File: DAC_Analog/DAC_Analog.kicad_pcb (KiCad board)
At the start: 2 copper layers, 100 x 100 mm, 146 parts, among them J1 SPDIF_RX_1, J2 SPDIF_RX_2, J3 SPDIF_RX_3, J4 SPDIF_RX_4, J5 I2C_IN, J6 OutR, J7 OutL, J8 Conn_01x06, J9 Conn_01x04, T1 DA103C, T2 DA103C, T3 DA103C, T4 DA103C, U1 ISO154x, U10 OPA627xx, U11 TC595002ECB, U12 TPS79318, U13 SRC4392, U14 TPS79333, U15 TPS79333, U16 REG104_DCQ, U17 PCM1792A, U18 DS90LV012ATMF, U19 LMK61E2, U2 OPA627xx, U3 OPA627xx, U4 REG104_DCQ, U5 OPA627xx, U6 TC595002ECB, U7 OPA627xx, U8 OPA627xx, U9 REG104_DCQ

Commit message: update footprint
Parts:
- J1, J2, J3, J4, J6, J7: footprint Yame_library:HE10_14-2C-2.54-MR -> Pin_Headers:Pin_Header_Straight_1x02_Pitch2.54mm
- J5, J9: footprint Yame_library:HE10_14-4C-2.54-MR -> Pin_Headers:Pin_Header_Straight_1x04_Pitch2.54mm
- J8: footprint Yame_library:HE10_14-6C-2.54-MR -> Pin_Headers:Pin_Header_Straight_1x06_Pitch2.54mm
- moved J3 43.2 mm to (130.0, 103.0)
- moved J9 35.3 mm to (153.0, 44.0)
- moved J4 21.9 mm to (154.0, 98.0)
- moved J2 10.0 mm to (136.0, 91.0)
- moved J5 4.00 mm to (131.0, 52.0)
- moved J8 3.67 mm to (135.0, 55.0)

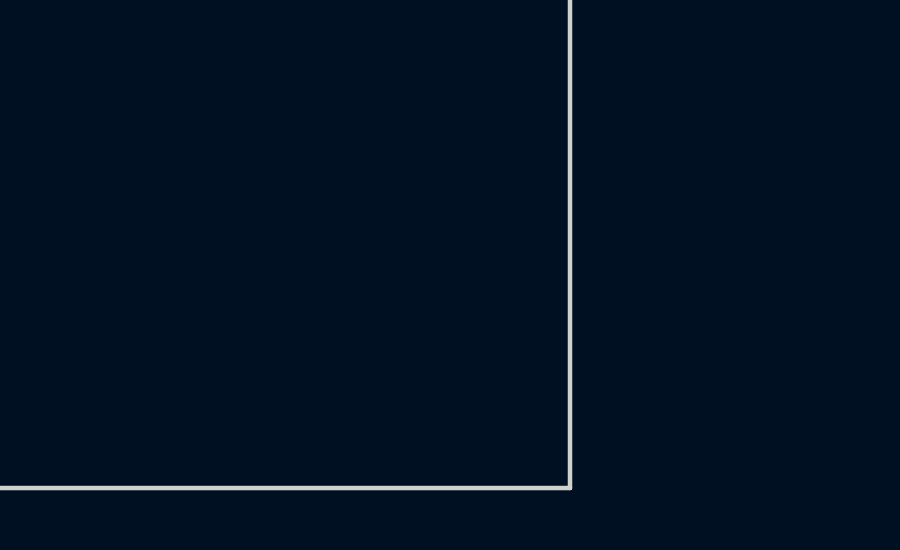
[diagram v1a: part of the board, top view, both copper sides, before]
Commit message: place all components on DAC_Analog
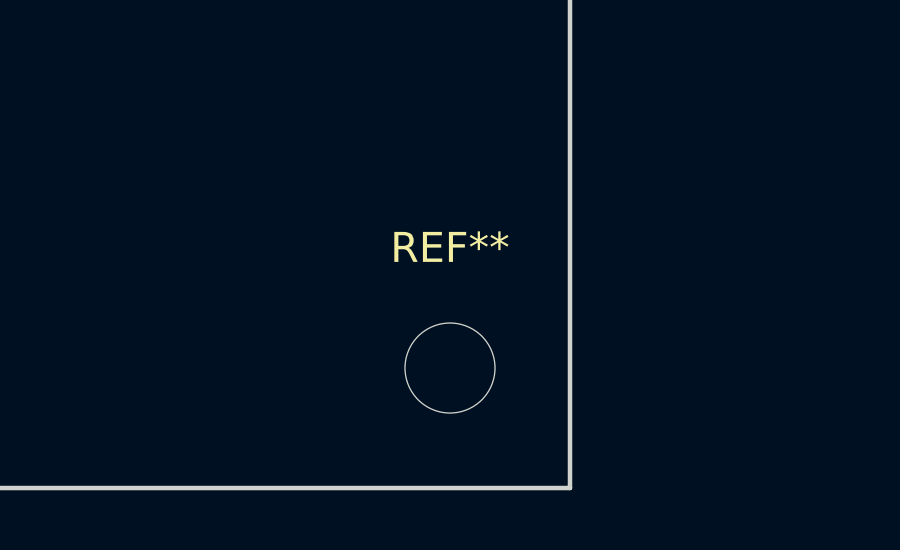
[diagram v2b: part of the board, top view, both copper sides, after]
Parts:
- added REF**: MountingHole_3mm, Mounting_Holes:MountingHole_3mm, F.Cu at (145.0, 145.0)
- J8: value Conn_01x06 -> Alim_DAC
- J9: value Conn_01x04 -> Alim_SRC
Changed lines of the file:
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@@
     (tracks 0)
     (zones 0)
-    (modules 146)
+    (modules 147)
     (nets 123)
   )
@@
       (effects (font (size 1 1) (thickness 0.15)))
     )
-    (fp_text value Conn_01x06 (at 0 15.03) (layer F.Fab)
+    (fp_text value Alim_DAC (at 0 15.03) (layer F.Fab)
       (effects (font (size 1 1) (thickness 0.15)))
     )
@@
       (effects (font (size 1 1) (thickness 0.15)))
     )
-    (fp_text value Conn_01x04 (at 0 9.95) (layer F.Fab)
+    (fp_text value Alim_SRC (at 0 9.95) (layer F.Fab)
       (effects (font (size 1 1) (thickness 0.15)))
     )
@@
     )
   )
+  (module Mounting_Holes:MountingHole_3mm (layer F.Cu)
+    (at 145 145)
+    (descr "Mounting Hole 3mm, no annular")
+    (tags "mounting hole 3mm no annular")
+    (attr virtual)
+    (fp_text reference REF** (at 0 -4) (layer F.SilkS)
+      (effects (font (size 1 1) (thickness 0.15)))
+    )
+    (fp_text value MountingHole_3mm (at 0 4) (layer F.Fab)
+      (effects (font (size 1 1) (thickness 0.15)))
+    )
+    (fp_text user %R (at 0.3 0) (layer F.Fab)
+      (effects (font (size 1 1) (thickness 0.15)))
+    )
+    (fp_circle (center 0 0) (end 3 0) (layer Cmts.User) (width 0.15))
+    (fp_circle (center 0 0) (end 3.25 0) (layer F.CrtYd) (width 0.05))
+    (pad 1 np_thru_hole circle (at 0 0) (size 3 3) (drill 3) (layers *.Cu *.Mask))
+  )
   (gr_line (start 49 149) (end 49 49) (angle 90) (layer Edge.Cuts) (width 0.15))

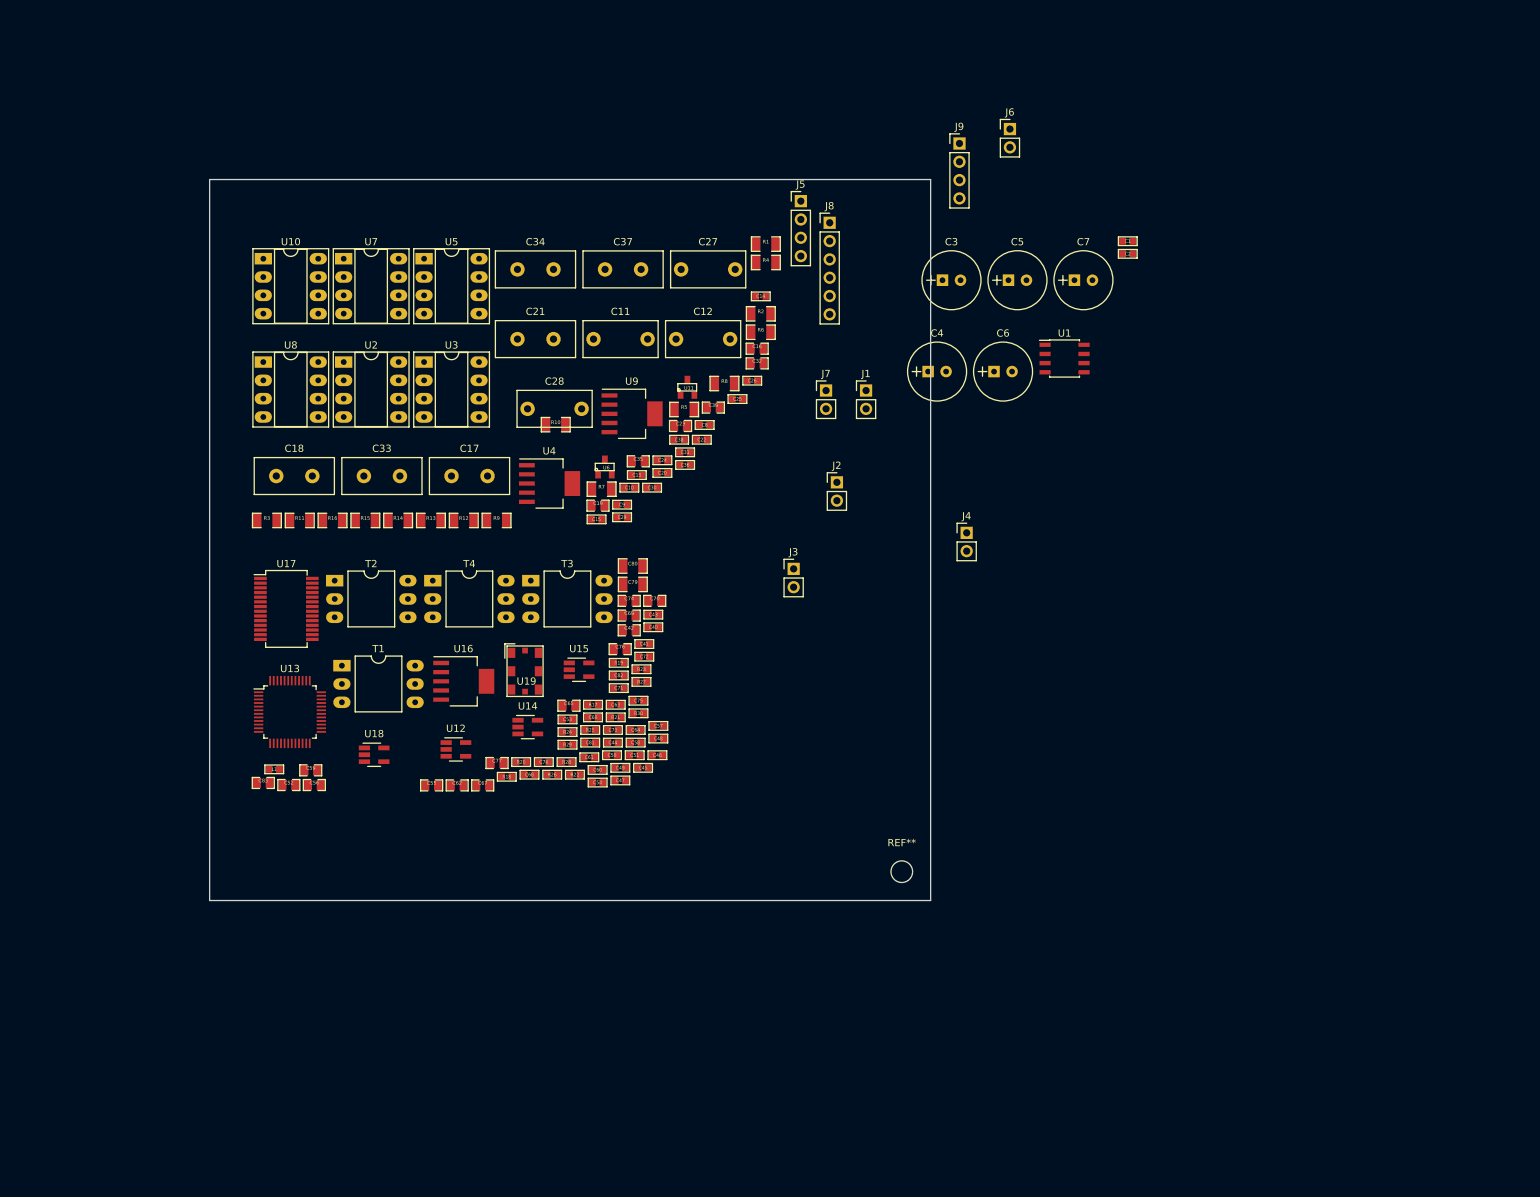
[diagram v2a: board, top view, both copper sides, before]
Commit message: Place cmp DAC_Analog
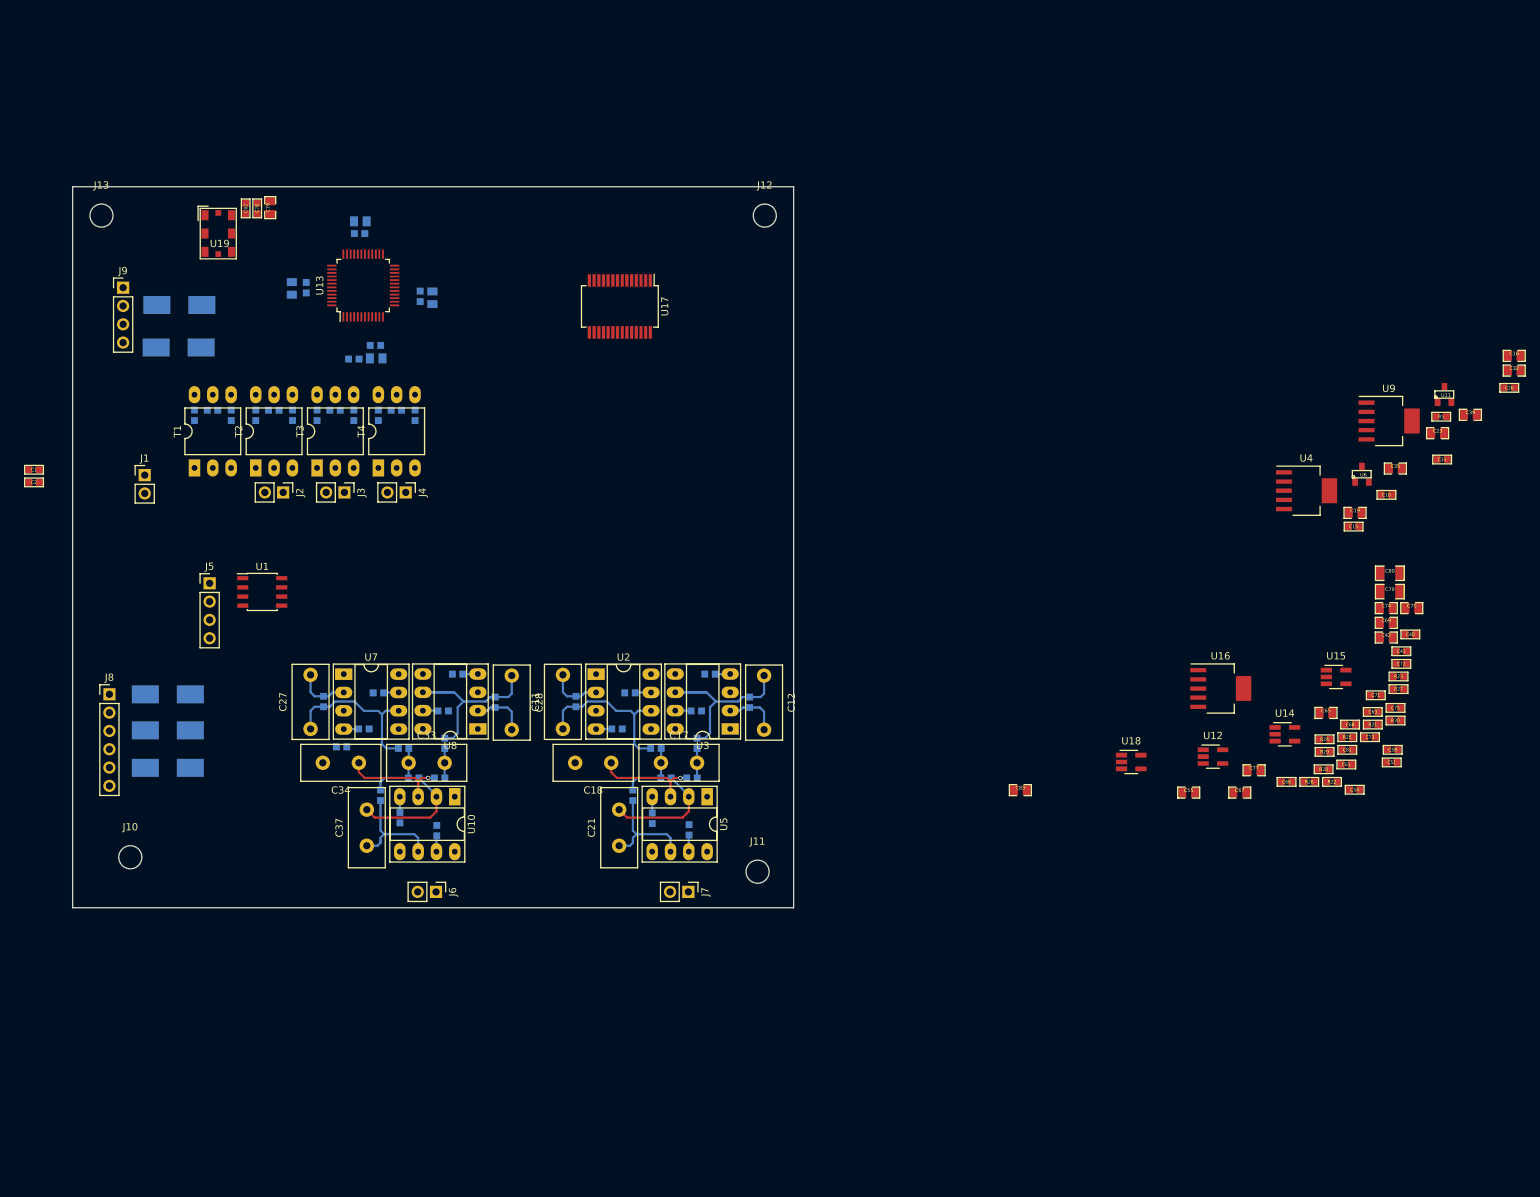
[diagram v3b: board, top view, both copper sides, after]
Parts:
- removed REF**: MountingHole_3mm, Mounting_Holes:MountingHole_3mm
- added J10: Fix, Mounting_Holes:MountingHole_3.2mm_M3, F.Cu at (38.0, 143.0)
- added J11: Fix, Mounting_Holes:MountingHole_3.2mm_M3, F.Cu at (125.0, 145.0)
- added J12: Fix, Mounting_Holes:MountingHole_3.2mm_M3, F.Cu at (126.0, 54.0)
- added J13: Fix, Mounting_Holes:MountingHole_3.2mm_M3, F.Cu at (34.0, 54.0)
- C13, C14, C20, C22, C24, C25, C29, C30, C36, C38, C43, C44, C45, C46, C47, C48, C49, C50, C52, C53, C56, C57, C59, C60, C62, C64, C8, C9, L1, R17, R18, R19, R20: moved to B.Cu
- C3, C4, C5, C6, C7: footprint Capacitors_THT:CP_Radial_Tantal_D8.0mm_P2.50mm -> Capacitors_Tantalum_SMD:CP_Tantalum_Case-C_EIA-6032-28_Hand; moved to B.Cu
- R1, R10, R11, R12, R13, R14, R15, R16, R2, R3, R4, R6, R7, R8, R9: footprint Yame_library:SM1206-MR -> Yame_library:SM0603-MR; moved to B.Cu
- R5: footprint Yame_library:SM1206-MR -> Yame_library:SM0603-MR
- moved C1 155.0 mm to (24.6, 89.3)
- moved C2 155.0 mm to (24.6, 91.0)
- moved C7 138.2 mm to (43.2, 120.4)
- moved J6 132.4 mm to (80.4, 147.8), turned to 270 degrees
- moved C6 124.9 mm to (43.2, 125.4)
- moved J8 119.4 mm to (35.1, 120.4)
- moved C4 118.9 mm to (43.2, 130.6)
- moved J9 117.7 mm to (37.0, 64.0)
- moved U1 115.9 mm to (56.3, 106.2)
- moved C5 115.0 mm to (44.8, 66.4)
- moved C3 106.4 mm to (44.7, 72.3)
- moved C16 105.0 mm to (229.9, 73.5)
- moved C23 105.0 mm to (219.3, 84.2)
- moved C32 105.0 mm to (229.9, 75.5)
- moved C42 105.0 mm to (212.2, 112.5)
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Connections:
- net Net-(J5-Pad2) renamed /scl_dig
- net Net-(J5-Pad3) renamed /sda_dig
- C1 pad 1: Net-(C1-Pad1) -> /vcc_dig
- C1 pad 2: Net-(C1-Pad2) -> /gnd_dig
- J5 pad 1: Net-(C1-Pad2) -> /vcc_dig
- J5 pad 4: Net-(C1-Pad1) -> /gnd_dig
- U1 pad 1: Net-(C1-Pad1) -> /vcc_dig
- U1 pad 4: Net-(C1-Pad2) -> /gnd_dig
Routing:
- net Net-(C12-Pad1): track 0.00 -> 27.7 mm
- net Net-(C28-Pad1): track 0.00 -> 26.9 mm
- net Net-(C27-Pad1): track 0.00 -> 22.8 mm
- net Net-(C11-Pad1): track 0.00 -> 22.8 mm
- net Net-(C37-Pad2): track 0.00 -> 16.1 mm
- net Net-(C21-Pad2): track 0.00 -> 16.1 mm
- net /Out_R: track 0.00 -> 15.2 mm
- net /Out_L: track 0.00 -> 15.2 mm
- net Net-(C34-Pad1): track 0.00 -> 14.6 mm, vias 0 -> 1
- net Net-(C18-Pad1): track 0.00 -> 14.6 mm, vias 0 -> 1
- net /Filter_Out/+5V_anlg: track 0.00 -> 12.9 mm
- net /Filter_Out/-5V_anlg: track 0.00 -> 12.7 mm
- net Net-(C33-Pad1): track 0.00 -> 9.32 mm
- net Net-(C17-Pad1): track 0.00 -> 9.32 mm
- net /IOUTR_P: track 0.00 -> 7.62 mm
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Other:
- net class Default: trace_width 0.25 -> 0.2

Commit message: Update layout
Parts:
- added D1: LED, Yame_library:SM0603-LED-MR, F.Cu at (32.1, 130.6)
- added D2: LED, Yame_library:SM0603-LED-MR, F.Cu at (33.7, 71.6)
- added D3: LED, Yame_library:SM0603-LED-MR, F.Cu at (32.1, 125.5)
- added D4: LED, Yame_library:SM0603-LED-MR, F.Cu at (33.7, 66.5)
- added D5: LED, Yame_library:SM0603-LED-MR, F.Cu at (32.1, 120.4)
- added J14: MCLK_Test, Pin_Headers:Pin_Header_Straight_1x02_Pitch2.54mm, F.Cu at (92.9, 74.0)
- added R31: R, Yame_library:SM0603-MR, F.Cu at (32.1, 131.9)
- added R32: R, Yame_library:SM0603-MR, F.Cu at (33.7, 73.0)
- added R33: R, Yame_library:SM0603-MR, F.Cu at (32.1, 126.9)
- added R34: R, Yame_library:SM0603-MR, F.Cu at (33.7, 67.9)
- added R35: R, Yame_library:SM0603-MR, F.Cu at (32.1, 121.8)
- added R36: R, Yame_library:SM0603-MR, F.Cu at (98.2, 75.5)
- added R37: R, Yame_library:SM0603-MR, F.Cu at (96.2, 74.0)
- C67, C69, C72, C73, C74, C75, C77, C81, U18: moved to B.Cu
- moved C75 128.0 mm to (88.0, 97.0), turned to 180 degrees
- moved C74 127.1 mm to (85.7, 96.0), turned to 270 degrees
- moved C71 127.0 mm to (87.5, 89.7), turned to 180 degrees
- moved C72 125.4 mm to (98.7, 67.7)
- moved C73 122.7 mm to (92.8, 89.7)
- moved R24 122.3 mm to (87.5, 88.2)
- moved C69 121.4 mm to (93.0, 87.8)
- moved C80 120.9 mm to (91.8, 104.5), turned to 90 degrees
- moved C79 118.5 mm to (94.2, 104.5), turned to 90 degrees
- moved R27 118.2 mm to (105.7, 72.2), turned to 270 degrees
- moved R28 116.8 mm to (89.8, 103.7), turned to 90 degrees
- moved R25 116.1 mm to (105.7, 69.3), turned to 270 degrees
- moved C67 115.4 mm to (98.7, 66.0)
- moved C81 113.2 mm to (98.0, 97.0)
- moved R26 112.9 mm to (107.0, 70.8), turned to 270 degrees
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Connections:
- U18 pad 5: /DigitalCv_DAC/MCK -> Net-(R36-Pad1)
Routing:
- net GNDD: track 0.00 -> 9.17 mm

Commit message: DAC_Analog : place all cmp
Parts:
- added R38: 2k2, Yame_library:SM0603-MR, F.Cu at (96.3, 55.1)
- added R39: 2k2, Yame_library:SM0603-MR, F.Cu at (98.7, 55.1)
- C26, C31, C32, R5, U9: moved to B.Cu
- moved C40 180.9 mm to (43.4, 56.7), turned to 270 degrees
- moved C51 174.7 mm to (53.1, 59.4), turned to 270 degrees
- moved C41 174.6 mm to (49.5, 56.7), turned to 270 degrees
- moved C42 173.0 mm to (49.7, 53.1), turned to 90 degrees
- moved C54 166.0 mm to (59.3, 59.4), turned to 270 degrees
- moved C16 162.5 mm to (72.5, 113.7)
- moved U12 159.9 mm to (46.5, 55.0)
- moved U14 157.5 mm to (56.2, 57.7)
- moved R23 148.6 mm to (77.5, 59.0), turned to 180 degrees
- moved C55 147.7 mm to (59.5, 55.9), turned to 90 degrees
- moved C61 146.8 mm to (77.5, 60.4)
- moved R21 139.9 mm to (83.8, 64.8), turned to 90 degrees
- moved R22 138.2 mm to (83.0, 67.0), turned to 180 degrees
- moved C58 135.5 mm to (84.3, 85.9), turned to 270 degrees
- moved C10 135.3 mm to (78.0, 110.6), turned to 90 degrees
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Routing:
- net Net-(C17-Pad2): track 3.24 -> 17.8 mm, vias 0 -> 2
- net Net-(C33-Pad2): track 4.09 -> 17.8 mm, vias 0 -> 2
- net Net-(C12-Pad1): track 27.7 -> 26.9 mm

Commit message: Update layout
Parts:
- moved C2 41.0 mm to (54.5, 63.4), turned to 180 degrees
- moved U1 37.4 mm to (53.4, 59.0), turned to 270 degrees
- moved C1 33.3 mm to (55.4, 53.8), turned to 90 degrees
- moved R39 29.8 mm to (89.5, 26.8), turned to 0 degrees
- moved R38 26.9 mm to (89.5, 29.1), turned to 0 degrees
- moved C51 10.9 mm to (51.1, 70.2)
- moved C54 10.9 mm to (57.3, 70.2)
- moved U14 10.9 mm to (54.2, 68.5)
- moved C55 10.8 mm to (54.5, 65.5), turned to 180 degrees
- moved C42 4.72 mm to (45.5, 55.2), turned to 180 degrees
- moved U12 3.53 mm to (45.0, 58.2)
- moved C40 3.53 mm to (41.9, 59.9)
- moved C41 3.53 mm to (48.0, 59.9)
- moved C53 1.76 mm to (72.5, 70.3)
- moved C57 0.65 mm to (63.0, 64.2)
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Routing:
- net /gnd_dig: track 0.00 -> 108.3 mm, vias 0 -> 1
- net /sda_dig: track 0.00 -> 103.7 mm, vias 0 -> 1
- net /scl_dig: track 0.00 -> 101.6 mm, vias 0 -> 1
- net /vcc_dig: track 0.00 -> 99.7 mm, vias 0 -> 1
- net Net-(C43-Pad1): track 0.00 -> 36.0 mm, vias 0 -> 1
- net Net-(C44-Pad1): track 0.00 -> 34.0 mm, vias 0 -> 1
- net /+3.3V_rcv: track 0.00 -> 31.7 mm, vias 0 -> 2
- net Net-(C45-Pad1): track 0.00 -> 28.6 mm, vias 0 -> 1
- net Net-(C46-Pad1): track 0.00 -> 26.5 mm, vias 0 -> 1
- net /+4v_dig: track 0.00 -> 22.8 mm, vias 0 -> 1
- net Net-(C47-Pad1): track 0.00 -> 21.0 mm, vias 0 -> 1
- net Net-(C48-Pad1): track 0.00 -> 19.0 mm, vias 0 -> 1
- net /+2v_dig: track 0.00 -> 18.9 mm, vias 0 -> 1
- net Net-(C50-Pad1): track 0.00 -> 17.5 mm, vias 0 -> 1
- net Net-(C49-Pad1): track 0.00 -> 15.6 mm, vias 0 -> 1
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
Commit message: Update layout
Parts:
- C26, C31, C32, U9: moved to F.Cu
- C61, R23: moved to B.Cu
- moved R38 42.5 mm to (58.7, 58.4), turned to 180 degrees
- moved R39 40.6 mm to (60.2, 55.0), turned to 180 degrees
- moved C10 8.95 mm to (69.1, 110.7)
- moved C31 6.10 mm to (117.0, 112.5), turned to 0 degrees
- moved C26 2.03 mm to (110.5, 109.4)
- moved U9 2.03 mm to (114.9, 107.0)
- moved C83 1.50 mm to (106.0, 105.5)
- moved C58 1.45 mm to (84.3, 84.5), turned to 90 degrees
- moved C60 0.65 mm to (69.8, 57.1)
- moved C72 0.40 mm to (98.2, 67.7)
- moved C32 0.36 mm to (113.9, 112.5), turned to 0 degrees
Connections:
- C13 pad 1: /Filter_Out/-5V_anlg -> /Filter_Out/-5V_anlg_L
- C14 pad 1: /Filter_Out/+5V_anlg -> /Filter_Out/+5V_anlg_L
- C20 pad 1: /Filter_Out/-5V_anlg -> /Filter_Out/-5V_anlg_L
- C22 pad 1: /Filter_Out/+5V_anlg -> /Filter_Out/+5V_anlg_L
- C32 pad 1: /Filter_Out/+5V_anlg -> /Filter_Out/+5V_anlg_L
- C35 pad 1: /Filter_Out/-5V_anlg -> /Filter_Out/-5V_anlg_L
- C8 pad 1: /Filter_Out/-5V_anlg -> /Filter_Out/-5V_anlg_L
- C9 pad 1: /Filter_Out/+5V_anlg -> /Filter_Out/+5V_anlg_L
- U11 pad 1: /Filter_Out/-5V_anlg -> /Filter_Out/-5V_anlg_L
- U2 pad 4: /Filter_Out/-5V_anlg -> /Filter_Out/-5V_anlg_L
- U2 pad 7: /Filter_Out/+5V_anlg -> /Filter_Out/+5V_anlg_L
- U3 pad 4: /Filter_Out/-5V_anlg -> /Filter_Out/-5V_anlg_L
- U3 pad 7: /Filter_Out/+5V_anlg -> /Filter_Out/+5V_anlg_L
- U5 pad 4: /Filter_Out/-5V_anlg -> /Filter_Out/-5V_anlg_L
- U5 pad 7: /Filter_Out/+5V_anlg -> /Filter_Out/+5V_anlg_L
- U9 pad 2: /Filter_Out/+5V_anlg -> /Filter_Out/+5V_anlg_L
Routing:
- net /+6v_anlg: track 0.00 -> 167.7 mm, vias 0 -> 9
- net /+3.3V_rcv: track 31.7 -> 195.9 mm, vias 2 -> 10
- net /DigitalCv_DAC/LRCK: track 0.00 -> 134.8 mm, vias 0 -> 2
- net /DigitalCv_DAC/DATA: track 0.00 -> 132.4 mm, vias 0 -> 4
- net /-6V_anlg: track 0.00 -> 129.0 mm, vias 0 -> 4
- net /DigitalCv_DAC/BCK: track 0.00 -> 127.8 mm, vias 0 -> 2
- net /SCL: track 0.00 -> 126.0 mm, vias 0 -> 6
- net /SDA: track 0.00 -> 120.8 mm, vias 0 -> 6
- net /+4v_anlg: track 0.00 -> 85.1 mm, vias 0 -> 1
- net /Filter_Out/-5V_anlg_L: track 0.00 -> 69.5 mm, vias 0 -> 4
- net /DigitalCv_DAC/+5V_dac: track 0.00 -> 65.3 mm, vias 0 -> 6
- net /DigitalCv_DAC/+1.8V_rcv: track 1.91 -> 65.6 mm, vias 0 -> 2
- net /Filter_Out/-5V_anlg: track 12.7 -> 68.7 mm, vias 0 -> 4
- net /IOUTR_N: track 7.46 -> 62.5 mm, vias 0 -> 1
- net /Filter_Out/+5V_anlg_L: track 0.00 -> 54.7 mm, vias 0 -> 3
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- added copper zone on B.Cu, net GND
- added copper zone on F.Cu, net GND
